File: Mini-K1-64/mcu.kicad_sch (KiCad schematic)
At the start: 19 parts, among them J2 Conn_01x16_Pin, J3 Conn_01x16_Pin, J4 Conn_01x16_Pin, J5 Conn_01x16_Pin, SW1 KEY, U2 FS32K144HAT0MLHT, Y1 8M

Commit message: Format PCB
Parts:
- renumbered C1 to C11, C2 to C12, C3 to C2, R2 to R1, R1 to R11, R11 to R2, R12 to R3, R7 to R4, R6 to R5, R3 to R7
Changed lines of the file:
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@@
 		(dnp no)
 		(fields_autoplaced yes)
-		(property "Reference" "C1"
+		(property "Reference" "C11"
 			(at 38.1 96.5199 0)
 			(effects
@@
 			(project "Mini-K1-64"
 				(path "/1a7e0d91-a6c0-4b42-a7c6-42574ab26c7c/7e8b3670-5aec-4076-8d2a-ba1c17fd4016"
-					(reference "C1")
+					(reference "C11")
 					(unit 1)
 				)
@@
 		(dnp no)
 		(fields_autoplaced yes)
-		(property "Reference" "C2"
+		(property "Reference" "C12"
 			(at 50.8 96.5199 0)
 			(effects
@@
 			(project "Mini-K1-64"
 				(path "/1a7e0d91-a6c0-4b42-a7c6-42574ab26c7c/7e8b3670-5aec-4076-8d2a-ba1c17fd4016"
-					(reference "C2")
+					(reference "C12")
 					(unit 1)
 				)
@@
 		(on_board yes)
 		(dnp no)
-		(property "Reference" "R7"
+		(property "Reference" "R4"
 			(at 58.42 37.338 90)
 			(effects
@@
 			(project "Mini-K1-64"
 				(path "/1a7e0d91-a6c0-4b42-a7c6-42574ab26c7c/7e8b3670-5aec-4076-8d2a-ba1c17fd4016"
-					(reference "R7")
+					(reference "R4")
 					(unit 1)
 				)
@@
 		(on_board yes)
 		(dnp no)
-		(property "Reference" "R3"
+		(property "Reference" "R7"
 			(at 58.166 47.498 90)
 			(effects
@@
 			(project "Mini-K1-64"
 				(path "/1a7e0d91-a6c0-4b42-a7c6-42574ab26c7c/7e8b3670-5aec-4076-8d2a-ba1c17fd4016"
-					(reference "R3")
+					(reference "R7")
 					(unit 1)
 				)
@@
 		(on_board yes)
 		(dnp no)
-		(property "Reference" "R6"
+		(property "Reference" "R5"
 			(at 55.118 121.92 90)
 			(effects
@@
 			(project "Mini-K1-64"
 				(path "/1a7e0d91-a6c0-4b42-a7c6-42574ab26c7c/7e8b3670-5aec-4076-8d2a-ba1c17fd4016"
-					(reference "R6")
+					(reference "R5")
 					(unit 1)
 				)
@@
 		(dnp no)
 		(fields_autoplaced yes)
-		(property "Reference" "C3"
+		(property "Reference" "C2"
 			(at 165.1 146.0499 0)
 			(effects
@@
 			(project "Mini-K1-64"
 				(path "/1a7e0d91-a6c0-4b42-a7c6-42574ab26c7c/7e8b3670-5aec-4076-8d2a-ba1c17fd4016"
-					(reference "C3")
+					(reference "C2")
 					(unit 1)
 				)
@@
 		(on_board yes)
 		(dnp no)
-		(property "Reference" "R2"
+		(property "Reference" "R1"
 			(at 58.42 43.942 90)
 			(effects
@@
 			(project "Mini-K1-64"
 				(path "/1a7e0d91-a6c0-4b42-a7c6-42574ab26c7c/7e8b3670-5aec-4076-8d2a-ba1c17fd4016"
-					(reference "R2")
+					(reference "R1")
 					(unit 1)
 				)
@@
 		(on_board yes)
 		(dnp no)
-		(property "Reference" "R12"
+		(property "Reference" "R3"
 			(at 57.15 90.932 90)
 			(effects
@@
 			(project "Mini-K1-64"
 				(path "/1a7e0d91-a6c0-4b42-a7c6-42574ab26c7c/7e8b3670-5aec-4076-8d2a-ba1c17fd4016"
-					(reference "R12")
+					(reference "R3")
 					(unit 1)
 				)
@@
 		(dnp no)
 		(fields_autoplaced yes)
-		(property "Reference" "R1"
+		(property "Reference" "R11"
 			(at 163.83 130.8099 0)
 			(effects
@@
 			(project "Mini-K1-64"
 				(path "/1a7e0d91-a6c0-4b42-a7c6-42574ab26c7c/7e8b3670-5aec-4076-8d2a-ba1c17fd4016"
-					(reference "R1")
+					(reference "R11")
 					(unit 1)
 				)
@@
 		(on_board yes)
 		(dnp no)
-		(property "Reference" "R11"
+		(property "Reference" "R2"
 			(at 56.896 84.328 90)
 			(effects
@@
 			(project "Mini-K1-64"
 				(path "/1a7e0d91-a6c0-4b42-a7c6-42574ab26c7c/7e8b3670-5aec-4076-8d2a-ba1c17fd4016"
-					(reference "R11")
+					(reference "R2")
 					(unit 1)
 				)

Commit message: Step Update
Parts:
- R15: value 0 -> 10K

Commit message: Rev0
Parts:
- renumbered J2 to J3, J3 to J4, J4 to J5, J5 to J6, R11 to R12, R14 to R15, R15 to R16
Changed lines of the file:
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@@
 		(dnp no)
 		(fields_autoplaced yes)
-		(property "Reference" "J3"
+		(property "Reference" "J4"
 			(at 240.665 74.93 0)
 			(effects
@@
 			(project "Mini-K1-64"
 				(path "/1a7e0d91-a6c0-4b42-a7c6-42574ab26c7c/7e8b3670-5aec-4076-8d2a-ba1c17fd4016"
-					(reference "J3")
+					(reference "J4")
 					(unit 1)
 				)
@@
 		(dnp no)
 		(fields_autoplaced yes)
-		(property "Reference" "J4"
+		(property "Reference" "J5"
 			(at 198.755 74.93 0)
 			(effects
@@
 			(project "Mini-K1-64"
 				(path "/1a7e0d91-a6c0-4b42-a7c6-42574ab26c7c/7e8b3670-5aec-4076-8d2a-ba1c17fd4016"
-					(reference "J4")
+					(reference "J5")
 					(unit 1)
 				)
@@
 		(on_board yes)
 		(dnp no)
-		(property "Reference" "R15"
+		(property "Reference" "R16"
 			(at 51.308 116.078 90)
 			(effects
@@
 			(project "Mini-K1-64"
 				(path "/1a7e0d91-a6c0-4b42-a7c6-42574ab26c7c/7e8b3670-5aec-4076-8d2a-ba1c17fd4016"
-					(reference "R15")
+					(reference "R16")
 					(unit 1)
 				)
@@
 		(on_board yes)
 		(dnp no)
-		(property "Reference" "J5"
+		(property "Reference" "J6"
 			(at 239.395 25.4 0)
 			(effects
@@
 			(project "Mini-K1-64"
 				(path "/1a7e0d91-a6c0-4b42-a7c6-42574ab26c7c/7e8b3670-5aec-4076-8d2a-ba1c17fd4016"
-					(reference "J5")
+					(reference "J6")
 					(unit 1)
 				)
@@
 		(dnp no)
 		(fields_autoplaced yes)
-		(property "Reference" "J2"
+		(property "Reference" "J3"
 			(at 198.755 25.4 0)
 			(effects
@@
 			(project "Mini-K1-64"
 				(path "/1a7e0d91-a6c0-4b42-a7c6-42574ab26c7c/7e8b3670-5aec-4076-8d2a-ba1c17fd4016"
-					(reference "J2")
+					(reference "J3")
 					(unit 1)
 				)
@@
 		(on_board yes)
 		(dnp no)
-		(property "Reference" "R14"
+		(property "Reference" "R15"
 			(at 51.308 118.618 90)
 			(effects
@@
 			(project "Mini-K1-64"
 				(path "/1a7e0d91-a6c0-4b42-a7c6-42574ab26c7c/7e8b3670-5aec-4076-8d2a-ba1c17fd4016"
-					(reference "R14")
+					(reference "R15")
 					(unit 1)
 				)
@@
 		(dnp no)
 		(fields_autoplaced yes)
-		(property "Reference" "R11"
+		(property "Reference" "R12"
 			(at 163.83 130.8099 0)
 			(effects
@@
 			(project "Mini-K1-64"
 				(path "/1a7e0d91-a6c0-4b42-a7c6-42574ab26c7c/7e8b3670-5aec-4076-8d2a-ba1c17fd4016"
-					(reference "R11")
+					(reference "R12")
 					(unit 1)
 				)

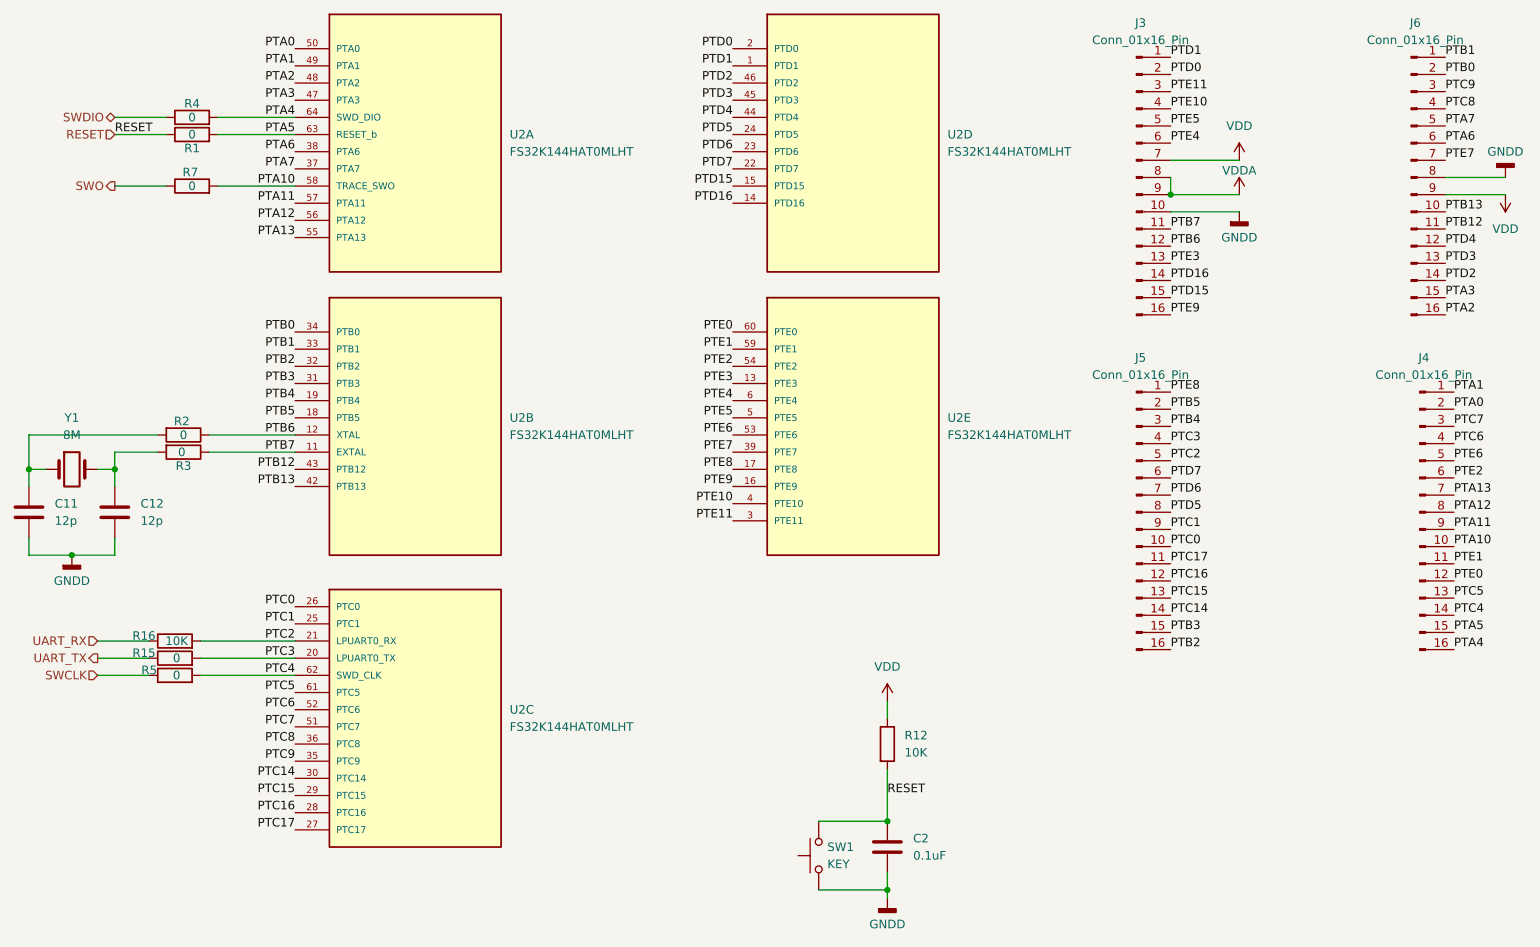
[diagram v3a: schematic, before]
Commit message: Update Debug Connector
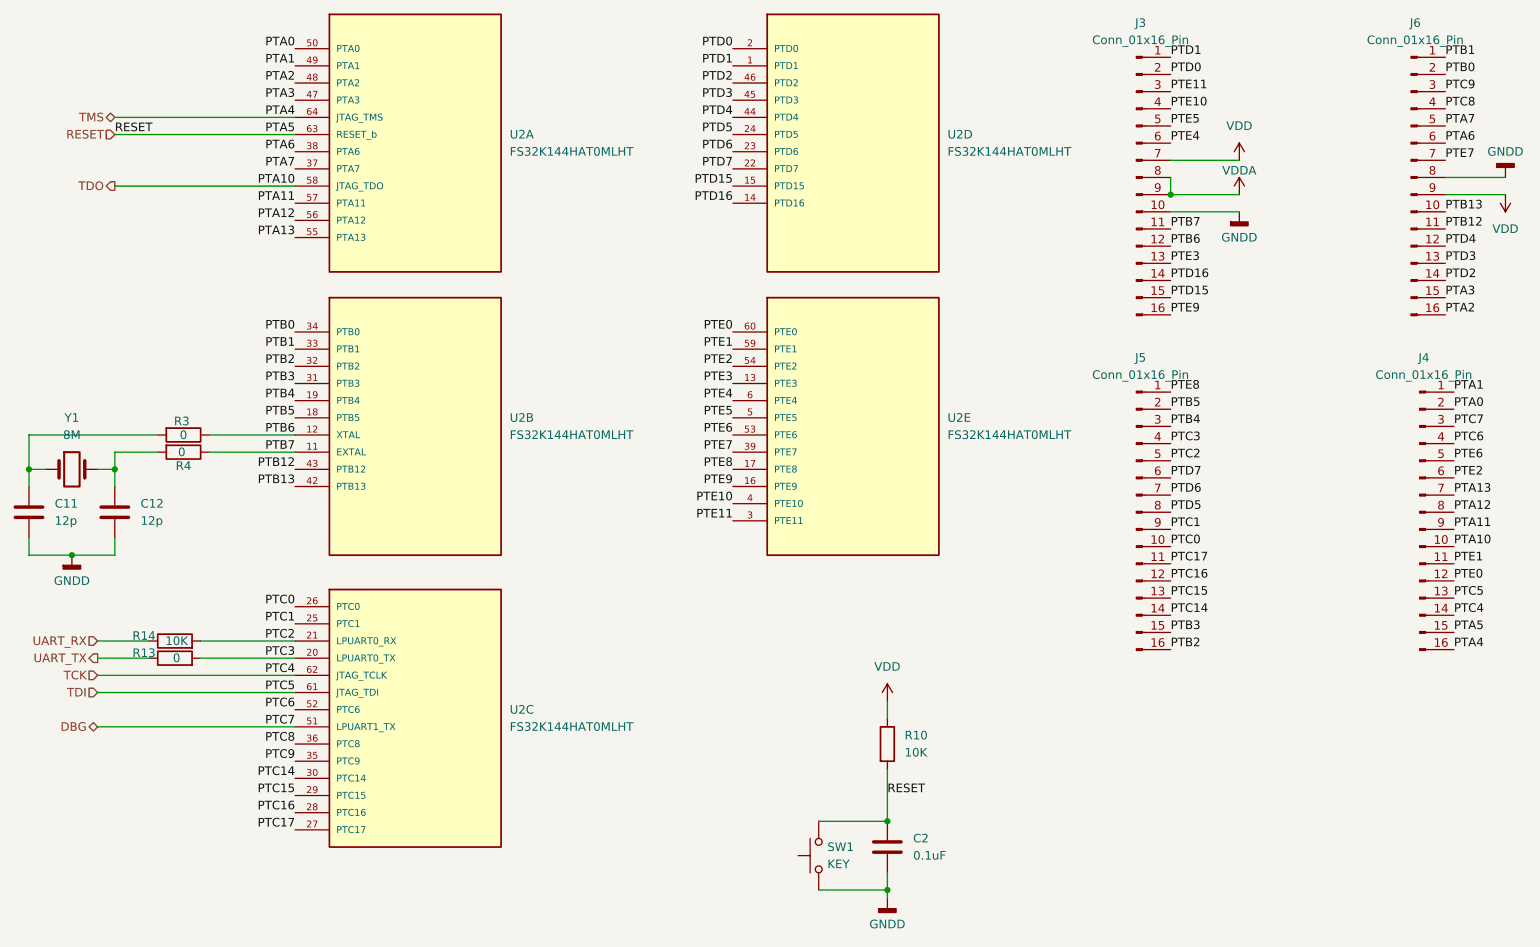
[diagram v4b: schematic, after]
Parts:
- removed R1, R4, R5, R7: 0, Resistor_SMD:R_0805_2012Metric, symbol Device:R
- renumbered R12 to R10, R15 to R13, R16 to R14, R2 to R3, R3 to R4
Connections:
- net PTA5 is gone; now on net RESET: J4.15 (Pin_15), U2.63 (PTA5)
- net PTA10 renamed TDO
- net PTA4 renamed TMS
- net PTC4 renamed TCK
- net PTC5 renamed TDI
- net PTC7 renamed DBG

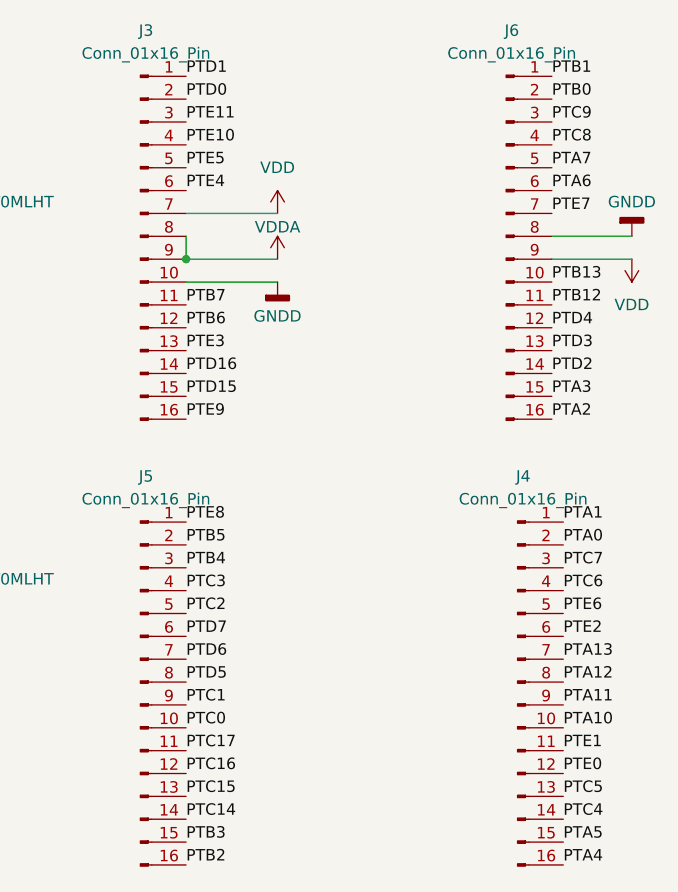
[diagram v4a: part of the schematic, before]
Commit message: Update to Kicad 9
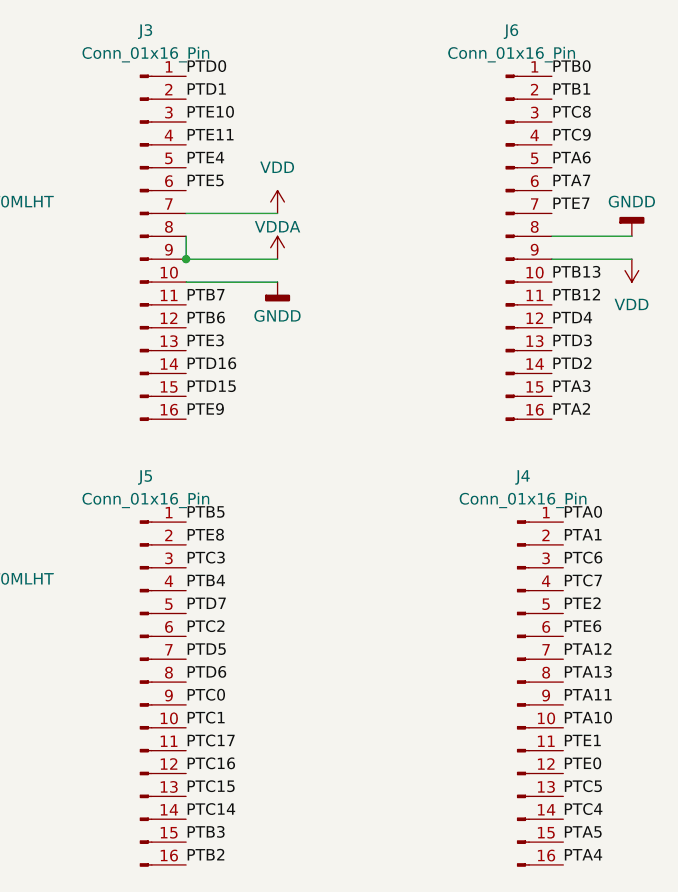
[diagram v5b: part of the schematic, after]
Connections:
- net DBG: now also J4.4 (Pin_4); no longer J4.3 (Pin_3)
- net PTA0: now also J4.1 (Pin_1); no longer J4.2 (Pin_2)
- net PTA1: now also J4.2 (Pin_2); no longer J4.1 (Pin_1)
- net PTA12: now also J4.7 (Pin_7); no longer J4.8 (Pin_8)
- net PTA13: now also J4.8 (Pin_8); no longer J4.7 (Pin_7)
- net PTA6: now also J6.5 (Pin_5); no longer J6.6 (Pin_6)
- net PTA7: now also J6.6 (Pin_6); no longer J6.5 (Pin_5)
- net PTB0: now also J6.1 (Pin_1); no longer J6.2 (Pin_2)
- net PTB1: now also J6.2 (Pin_2); no longer J6.1 (Pin_1)
- net PTB4: now also J5.4 (Pin_4); no longer J5.3 (Pin_3)
- net PTB5: now also J5.1 (Pin_1); no longer J5.2 (Pin_2)
- net PTC0: now also J5.9 (Pin_9); no longer J5.10 (Pin_10)
- net PTC1: now also J5.10 (Pin_10); no longer J5.9 (Pin_9)
- net PTC2: now also J5.6 (Pin_6); no longer J5.5 (Pin_5)
- net PTC3: now also J5.3 (Pin_3); no longer J5.4 (Pin_4)
- net PTC6: now also J4.3 (Pin_3); no longer J4.4 (Pin_4)
- net PTC8: now also J6.3 (Pin_3); no longer J6.4 (Pin_4)
- net PTC9: now also J6.4 (Pin_4); no longer J6.3 (Pin_3)
- net PTD0: now also J3.1 (Pin_1); no longer J3.2 (Pin_2)
- net PTD1: now also J3.2 (Pin_2); no longer J3.1 (Pin_1)
- net PTD5: now also J5.7 (Pin_7); no longer J5.8 (Pin_8)
- net PTD6: now also J5.8 (Pin_8); no longer J5.7 (Pin_7)
- net PTD7: now also J5.5 (Pin_5); no longer J5.6 (Pin_6)
- net PTE10: now also J3.3 (Pin_3); no longer J3.4 (Pin_4)
- net PTE11: now also J3.4 (Pin_4); no longer J3.3 (Pin_3)
- net PTE2: now also J4.5 (Pin_5); no longer J4.6 (Pin_6)
- net PTE4: now also J3.5 (Pin_5); no longer J3.6 (Pin_6)
- net PTE5: now also J3.6 (Pin_6); no longer J3.5 (Pin_5)
- net PTE6: now also J4.6 (Pin_6); no longer J4.5 (Pin_5)
- net PTE8: now also J5.2 (Pin_2); no longer J5.1 (Pin_1)
